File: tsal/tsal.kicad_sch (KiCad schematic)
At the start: 21 parts, among them J1 Conn_01x04, J2 Conn_01x03, J3 Conn_01x04, J4 Conn_01x02, Q1 FDN359BN, Q2 FDN359BN, Q3 FDN359BN, U1 4001, U2 40106

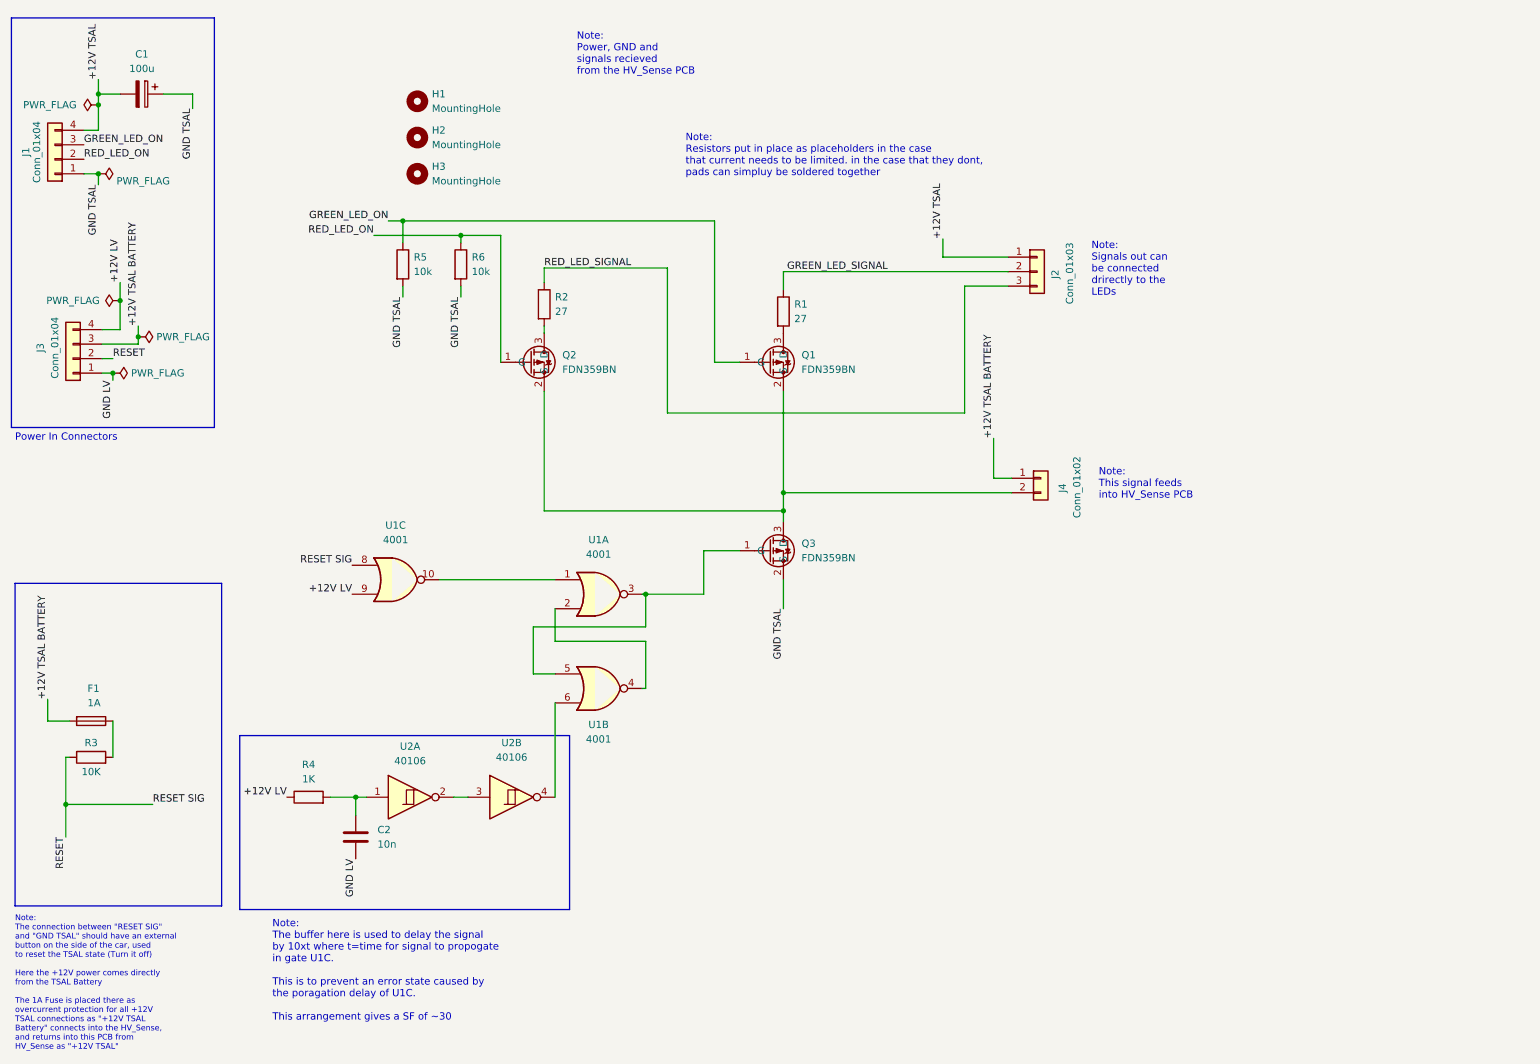
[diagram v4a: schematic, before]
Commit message: fix(tsal): corrected a few power connection issues
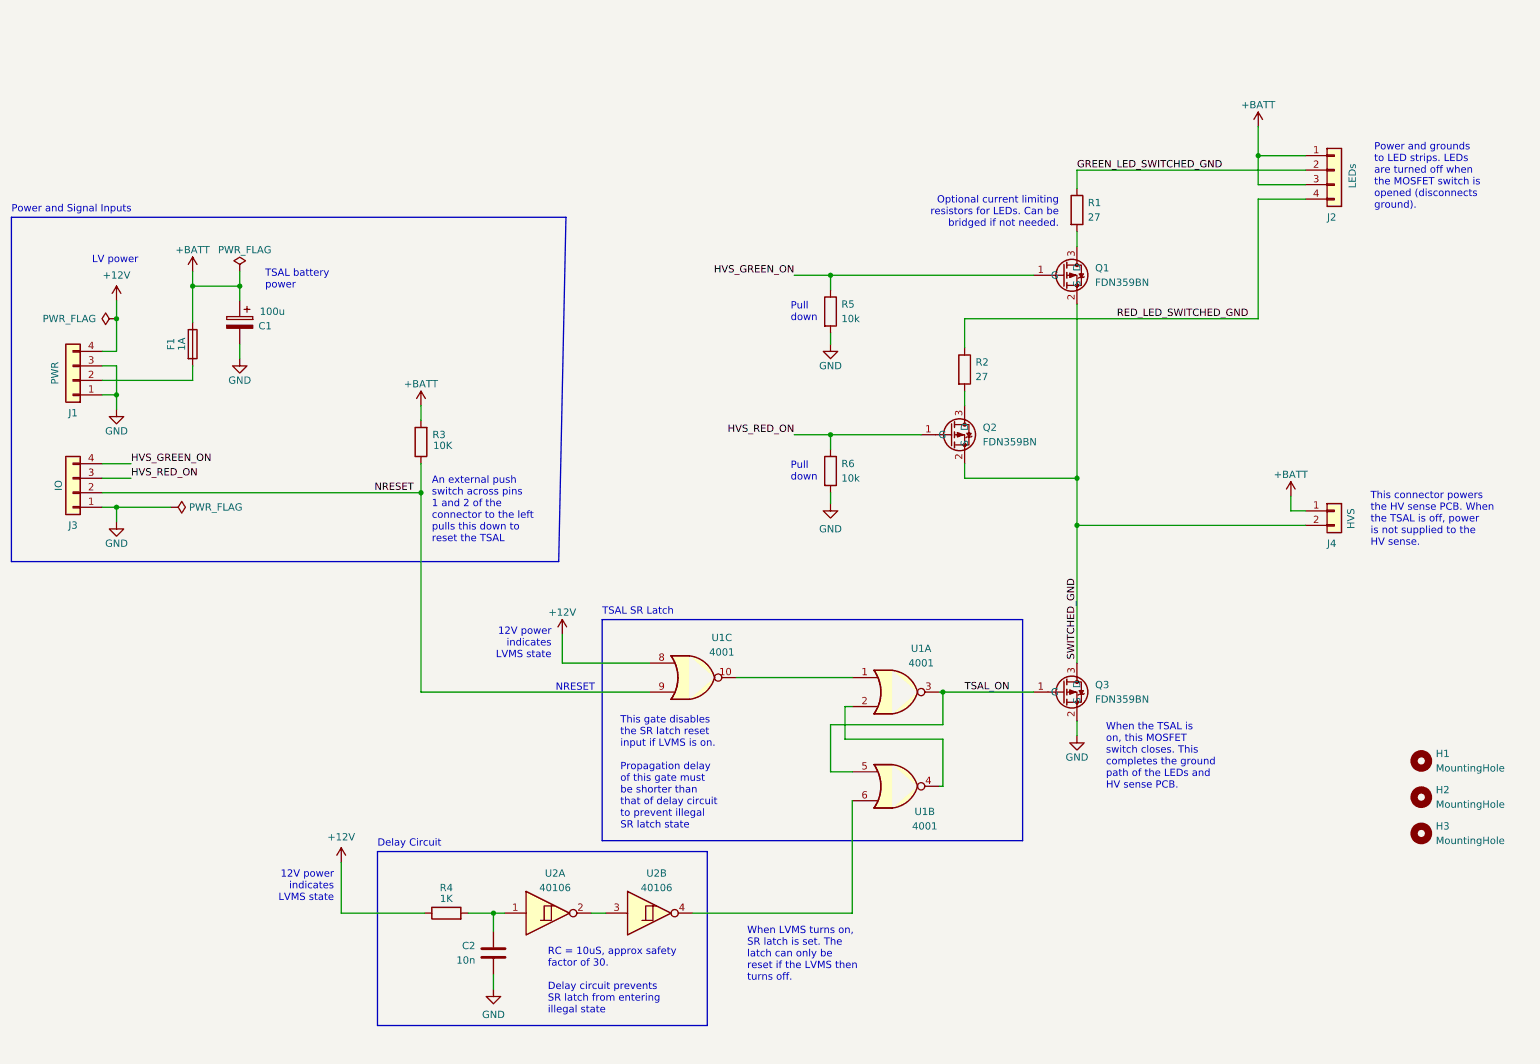
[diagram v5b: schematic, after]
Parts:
- removed J2: Conn_01x03, Connector_Molex:Molex_Micro-Fit_3.0_43650-0315_1x03_P3.00mm_Vertical, symbol Connector_Generic:Conn_01x03
- added J2: LEDs, symbol Connector_Generic:Conn_01x04
- J1: value Conn_01x04 -> PWR
- J3: value Conn_01x04 -> IO
- J4: value Conn_01x02 -> HVS
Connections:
- net SWITCHED_GND: now reaches J4.2 (Pin_2), Q1.2 (S), Q2.2 (S), Q3.3 (D)
- net TSAL_ON: now reaches Q3.1 (G), U1.3, U1.5
- net +BATT: now reaches F1.1, R3.2
- net +BATT: now also C1.1, J4.1 (Pin_1), J2.1 (Pin_1), J2.3 (Pin_3)
- removed net +12V LV: J3.4 (Pin_4), R4.1, U1.9
- net +12V TSAL renamed +12V
- net +12V: now also R4.1, U1.8; no longer C1.2
- removed net +12V TSAL BATTERY: F1.2, J3.3 (Pin_3), J4.1 (Pin_1)
- net GND LV renamed GND
- net GND: now also C1.2, J1.1 (Pin_1), J1.3 (Pin_3), Q3.2 (S), R5.2, R6.2
- removed net GND TSAL: C1.1, J1.1 (Pin_1), Q3.2 (S), R5.2, R6.2
- net GREEN_LED_ON renamed HVS_GREEN_ON
- net HVS_GREEN_ON: now also J3.4 (Pin_4); no longer J1.3 (Pin_3)
- net GREEN_LED_SIGNAL renamed GREEN_LED_SWITCHED_GND
- net GREEN_LED_SWITCHED_GND: now also J2.2 (Pin_2)
- net RED_LED_ON renamed HVS_RED_ON
- net HVS_RED_ON: now also J3.3 (Pin_3); no longer J1.2 (Pin_2)
- net RED_LED_SIGNAL renamed RED_LED_SWITCHED_GND
- net RED_LED_SWITCHED_GND: now also J2.4 (Pin_4)
- net RESET renamed NRESET
- net NRESET: now also U1.9; no longer U1.8
- new net: F1.2, J1.2 (Pin_2)
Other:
- note added: "12V power indicates LVMS state"
- note added: "An external push switch across pins 1 and 2 of the connector to the left pulls this down to reset the TSAL"
- note added: "Delay Circuit"
- note added: "LV power"
- note added: "NRESET"
- note added: "Optional current limiting resistors for LEDs. Can be bridged if not needed."
- note added: "Power and Signal Inputs"
- note added: "Power and grounds to LED strips. LEDs are turned off when the MOSFET switch is opened (disconnects ground)."
- note added: "Pull down"
- note added: "RC = 10uS, approx safety factor of 30. Delay circuit prevents SR latch from entering illegal state"
- note added: "TSAL SR Latch"
- note added: "TSAL battery power"
- note added: "This connector powers the HV sense PCB. When the TSAL is off, power is not supplied to the HV sense."
- note added: "This gate disables the SR latch reset input if LVMS is on. Propagation delay of this gate must be shorter than that of delay circuit to prevent illegal SR latch state"
- note added: "When LVMS turns on, SR latch is set. The latch can only be reset if the LVMS then turns off."
- note added: "When the TSAL is on, this MOSFET switch closes. This completes the ground path of the LEDs and HV sense PCB."
- note removed: "Note: Power, GND and signals recieved from the HV_Sense PCB"
- note removed: "Note: Resistors put in place as placeholders in the case that current needs to be limited. in the case that they dont, pads can simpluy be soldered together"
- note removed: "Note: Signals out can be connected drirectly to the LEDs"
- note removed: "Note: The buffer here is used to delay the signal by 10xt where t=time for signal to propogate in gate U1C. This is to prevent an error state caused by the poragation delay of U1C. This arrangement gives a SF of ~30"
- note removed: "Note: The connection between "RESET SIG" and "GND TSAL" should have an external button on the side of the car, used to reset the TSAL state (Turn it off) Here the +12V power comes directly from the TSAL Battery The 1A Fuse is placed there as overcurrent protection for all +12V TSAL connections as "+12V TSAL Battery" connects into the HV_Sense, and returns into this PCB from HV_Sense as "+12V TSAL""
- note removed: "Note: This signal feeds into HV_Sense PCB"
- note removed: "Power In Connectors"
- moved on the sheet: C2, H1, H2, H3, J1, J3, J4, Q1, Q2, Q3, R1, R2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

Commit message: fix(tsal): update layout with schematic changes
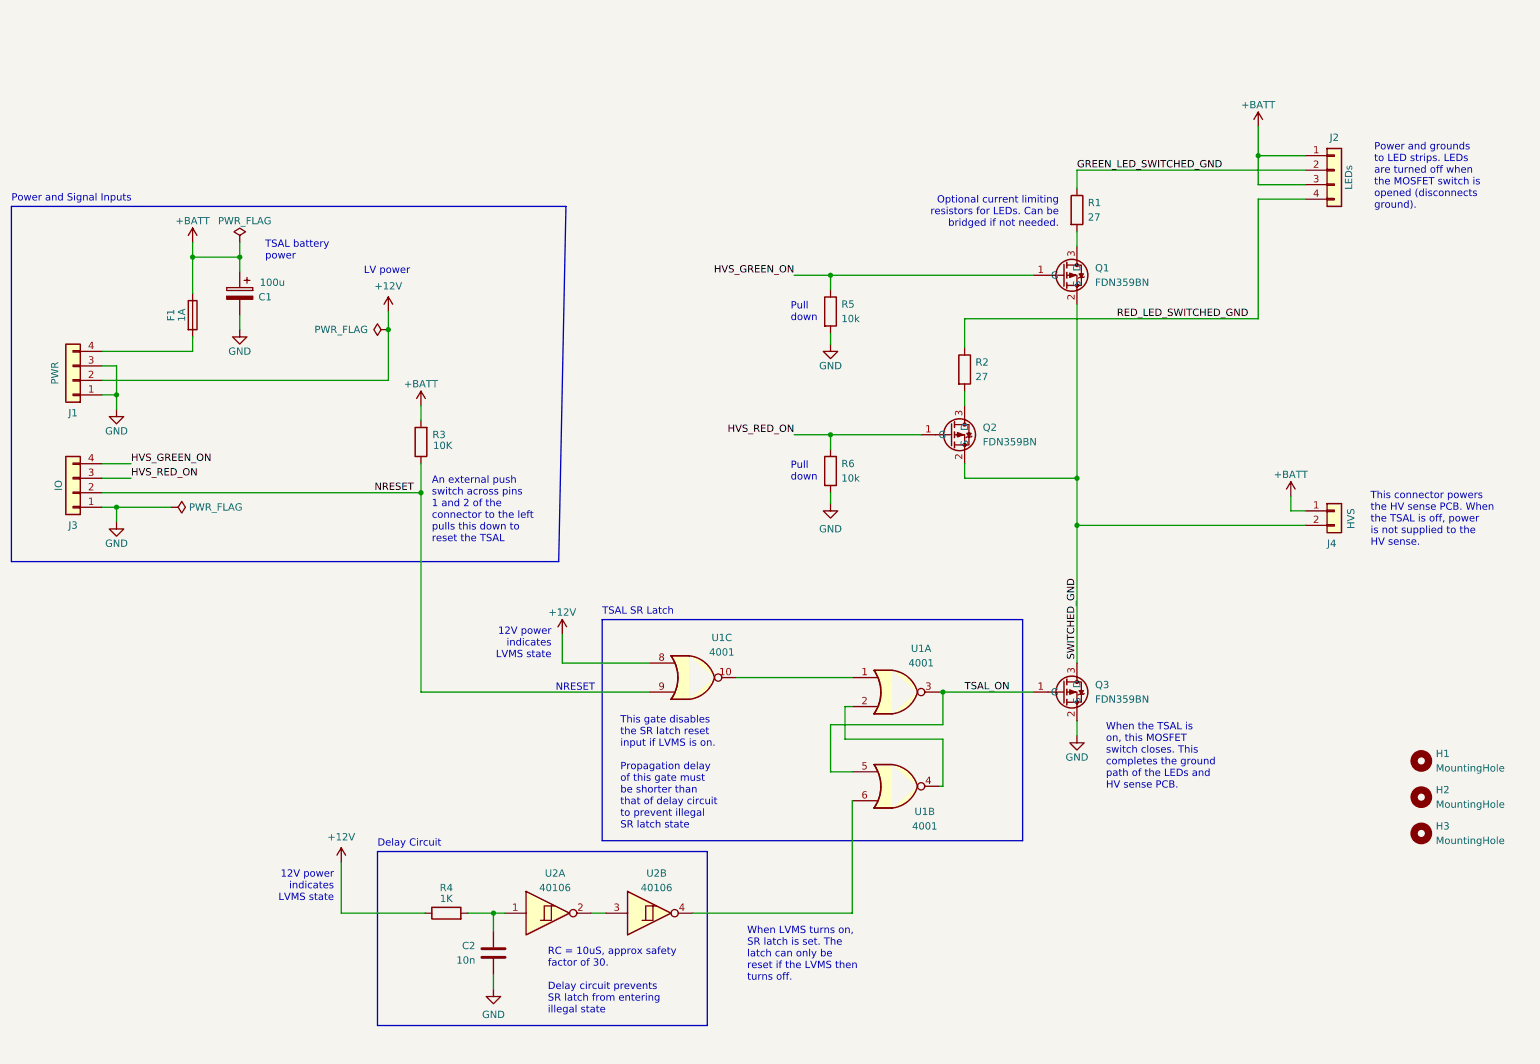
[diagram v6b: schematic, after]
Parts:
- J2: footprint (none) -> Connector_Molex:Molex_Micro-Fit_3.0_43650-0415_1x04_P3.00mm_Vertical; Supplier (none) -> TE
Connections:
- net +12V: now also J1.2 (Pin_2); no longer J1.4 (Pin_4)
- net at F1.2: now also J1.4 (Pin_4); no longer J1.2 (Pin_2)
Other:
- moved on the sheet: C1, F1

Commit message: feat(tsal): finalise layout
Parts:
- added C3, C4: 100n, Capacitor_SMD:C_0805_2012Metric_Pad1.18x1.45mm_HandSolder, symbol Device:C
- added unit 5 of U1
- added unit 7 of U2
- U2: footprint Package_SO:SO-14_3.9x8.65mm_P1.27mm -> Package_SO:SOIC-14_3.9x8.7mm_P1.27mm; Order Number 771-HEF40106BTD-T -> (none); Supplier Mouser -> (none)
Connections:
- net +BATT: now also C3.1, C4.1, U1.14 (VDD), U2.14 (VDD)
- net GND: now also C3.2, C4.2, U1.7 (VSS), U2.7 (VSS)

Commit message: feat(tsal): Added some 3D models
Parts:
- U2: Order Number (none) -> 771-HEF40106BTD-T; Supplier (none) -> Mouser
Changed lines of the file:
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@@
+      (effects (font (size 1.27 1.27)) hide)
+    )
+    (property "Order Number" "771-HEF40106BTD-T" (id 4) (at 109.855 170.815 0)
+      (effects (font (size 1.27 1.27)) hide)
+    )
+    (property "Supplier" "Mouser" (id 5) (at 109.855 170.815 0)
       (effects (font (size 1.27 1.27)) hide)
     )
@@
       (effects (font (size 1.27 1.27)) hide)
     )
+    (property "Order Number" "771-HEF40106BTD-T" (id 4) (at 67.945 135.89 0)
+      (effects (font (size 1.27 1.27)) hide)
+    )
+    (property "Supplier" "Mouser" (id 5) (at 67.945 135.89 0)
+      (effects (font (size 1.27 1.27)) hide)
+    )
     (pin "1")
     (pin "2")
@@
       (effects (font (size 1.27 1.27)) hide)
     )
+    (property "Order Number" "771-HEF40106BTD-T" (id 4) (at 127.635 170.815 0)
+      (effects (font (size 1.27 1.27)) hide)
+    )
+    (property "Supplier" "Mouser" (id 5) (at 127.635 170.815 0)
+      (effects (font (size 1.27 1.27)) hide)
+    )
